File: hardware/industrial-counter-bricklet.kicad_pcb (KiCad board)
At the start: 2 copper layers, 40 x 40 mm, 44 parts, among them J1 DEBUG, P1 CON-SENSOR2, P2 BOOT, P3 CONN_8, U1 XMC1XXX48, U2 TLP2767, U3 TLP2767, U4 TLP2767, U5 TLP2767, U6 DRILL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

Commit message: change opto type
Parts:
- U2, U3, U4, U5: value TLP2767 -> TLP2367
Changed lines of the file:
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@@
       (effects (font (size 0.15 0.15) (thickness 0.0375)))
     )
-    (fp_text value TLP2767 (at 0 -0.5) (layer F.Fab)
+    (fp_text value TLP2367 (at 0 -0.5) (layer F.Fab)
       (effects (font (size 0.15 0.15) (thickness 0.0375)))
     )
@@
       (effects (font (size 0.15 0.15) (thickness 0.0375)))
     )
-    (fp_text value TLP2767 (at 0 -0.5) (layer F.Fab)
+    (fp_text value TLP2367 (at 0 -0.5) (layer F.Fab)
       (effects (font (size 0.15 0.15) (thickness 0.0375)))
     )
@@
       (effects (font (size 0.15 0.15) (thickness 0.0375)))
     )
-    (fp_text value TLP2767 (at 0 -0.5) (layer F.Fab)
+    (fp_text value TLP2367 (at 0 -0.5) (layer F.Fab)
       (effects (font (size 0.15 0.15) (thickness 0.0375)))
     )
@@
       (effects (font (size 0.15 0.15) (thickness 0.0375)))
     )
-    (fp_text value TLP2767 (at 0 -0.5) (layer F.Fab)
+    (fp_text value TLP2367 (at 0 -0.5) (layer F.Fab)
       (effects (font (size 0.15 0.15) (thickness 0.0375)))
     )

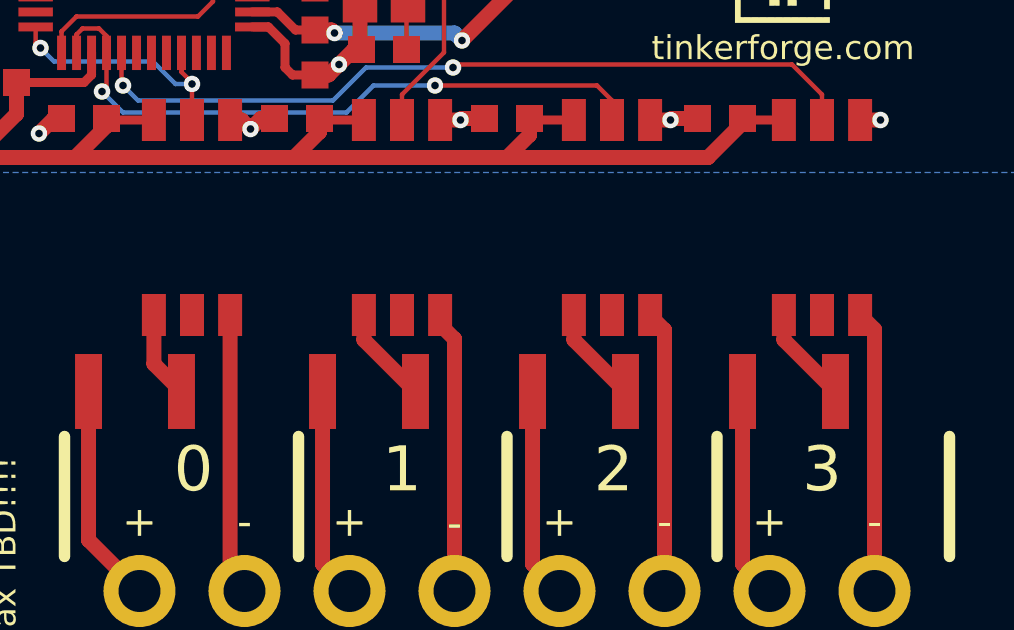
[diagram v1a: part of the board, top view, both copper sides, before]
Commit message: fix tlp2367 footprints
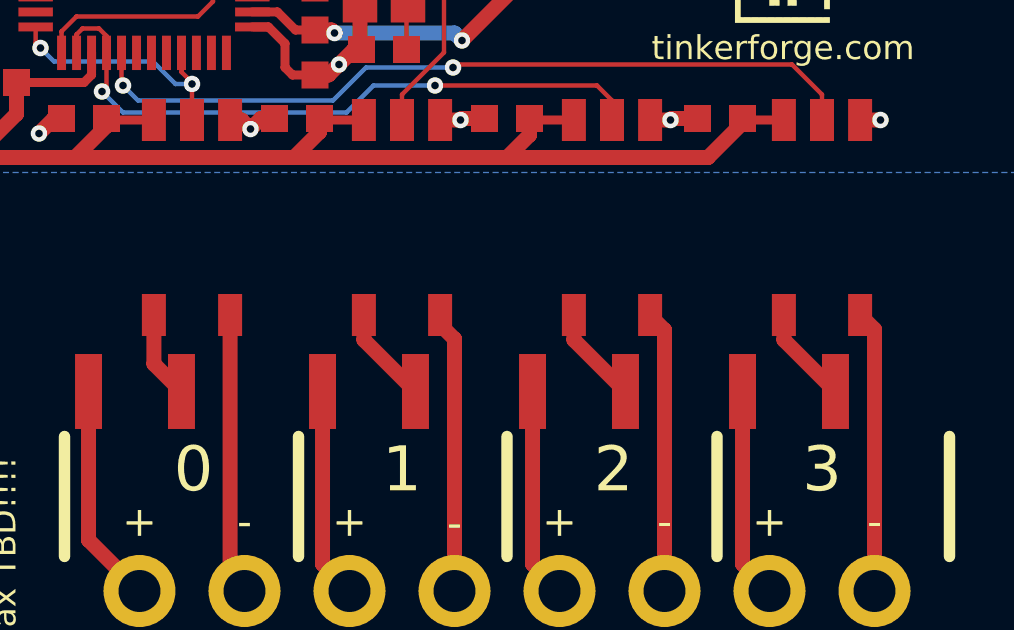
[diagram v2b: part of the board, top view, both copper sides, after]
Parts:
- U2, U3, U4, U5: footprint kicad-libraries:SO-6 -> kicad-libraries:SO-5
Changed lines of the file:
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@@
       (net 40 "Net-(J1-Pad1)"))
   )
-  (module kicad-libraries:SO-6 (layer Front)
+  (module kicad-libraries:SO-5 (layer Front)
+    (at 128.3 57.55)
+    (attr smd)
+    (fp_text reference U5 (at 0 0.5) (layer F.Fab)
+      (effects (font (size 0.15 0.15) (thickness 0.0375)))
+    )
+    (fp_text value TLP2367 (at 0 -0.5) (layer F.Fab)
+      (effects (font (size 0.15 0.15) (thickness 0.0375)))
+    )
+    (fp_circle (center -1.3 1.8) (end -1.2 1.9) (layer F.Fab) (width 0.15))
+    (fp_line (start -1.9 -2.3) (end 1.9 -2.3) (layer F.Fab) (width 0.15))
+    (fp_line (start 1.9 -2.3) (end 1.9 2.3) (layer F.Fab) (width 0.15))
+    (fp_line (start 1.9 2.3) (end -1.9 2.3) (layer F.Fab) (width 0.15))
+    (fp_line (start -1.9 2.3) (end -1.9 -2.3) (layer F.Fab) (width 0.15))
+    (pad 3 smd rect (at 1.27 3.25) (size 0.8 1.4) (layers Front F.Paste F.Mask)
+      (net 22 "Net-(P3-Pad8)"))
+    (pad 1 smd rect (at -1.27 3.25) (size 0.8 1.4) (layers Front F.Paste F.Mask)
+      (net 27 "Net-(R5-Pad2)"))
+    (pad 4 smd rect (at 1.27 -3.25) (size 0.8 1.4) (layers Front F.Paste F.Mask)
+      (net 1 GND))
+    (pad 5 smd rect (at 0 -3.25) (size 0.8 1.4) (layers Front F.Paste F.Mask)
+      (net 39 IN4))
+    (pad 6 smd rect (at -1.27 -3.25) (size 0.8 1.4) (layers Front F.Paste F.Mask)
+      (net 3 VCC))
+  )
+  (module kicad-libraries:SO-5 (layer Front)
+    (at 121.3 57.55)
+    (attr smd)
+    (fp_text reference U4 (at 0 0.5) (layer F.Fab)
+      (effects (font (size 0.15 0.15) (thickness 0.0375)))
+    )
+    (fp_text value TLP2367 (at 0 -0.5) (layer F.Fab)
+      (effects (font (size 0.15 0.15) (thickness 0.0375)))
+    )
+    (fp_circle (center -1.3 1.8) (end -1.2 1.9) (layer F.Fab) (width 0.15))
+    (fp_line (start -1.9 -2.3) (end 1.9 -2.3) (layer F.Fab) (width 0.15))
+    (fp_line (start 1.9 -2.3) (end 1.9 2.3) (layer F.Fab) (width 0.15))
+    (fp_line (start 1.9 2.3) (end -1.9 2.3) (layer F.Fab) (width 0.15))
+    (fp_line (start -1.9 2.3) (end -1.9 -2.3) (layer F.Fab) (width 0.15))
+    (pad 3 smd rect (at 1.27 3.25) (size 0.8 1.4) (layers Front F.Paste F.Mask)
+      (net 20 "Net-(P3-Pad6)"))
+    (pad 1 smd rect (at -1.27 3.25) (size 0.8 1.4) (layers Front F.Paste F.Mask)
+      (net 26 "Net-(R4-Pad2)"))
+    (pad 4 smd rect (at 1.27 -3.25) (size 0.8 1.4) (layers Front F.Paste F.Mask)
+      (net 1 GND))
+    (pad 5 smd rect (at 0 -3.25) (size 0.8 1.4) (layers Front F.Paste F.Mask)
+      (net 38 IN3))
+    (pad 6 smd rect (at -1.27 -3.25) (size 0.8 1.4) (layers Front F.Paste F.Mask)
+      (net 3 VCC))
+  )
+  (module kicad-libraries:SO-5 (layer Front)
+    (at 114.3 57.55)
+    (attr smd)
+    (fp_text reference U3 (at 0 0.5) (layer F.Fab)
+      (effects (font (size 0.15 0.15) (thickness 0.0375)))
+    )
+    (fp_text value TLP2367 (at 0 -0.5) (layer F.Fab)
+      (effects (font (size 0.15 0.15) (thickness 0.0375)))
+    )
+    (fp_circle (center -1.3 1.8) (end -1.2 1.9) (layer F.Fab) (width 0.15))
+    (fp_line (start -1.9 -2.3) (end 1.9 -2.3) (layer F.Fab) (width 0.15))
+    (fp_line (start 1.9 -2.3) (end 1.9 2.3) (layer F.Fab) (width 0.15))
+    (fp_line (start 1.9 2.3) (end -1.9 2.3) (layer F.Fab) (width 0.15))
+    (fp_line (start -1.9 2.3) (end -1.9 -2.3) (layer F.Fab) (width 0.15))
+    (pad 3 smd rect (at 1.27 3.25) (size 0.8 1.4) (layers Front F.Paste F.Mask)
+      (net 17 "Net-(P3-Pad4)"))
+    (pad 1 smd rect (at -1.27 3.25) (size 0.8 1.4) (layers Front F.Paste F.Mask)
+      (net 25 "Net-(R3-Pad2)"))
+    (pad 4 smd rect (at 1.27 -3.25) (size 0.8 1.4) (layers Front F.Paste F.Mask)
+      (net 1 GND))
+    (pad 5 smd rect (at 0 -3.25) (size 0.8 1.4) (layers Front F.Paste F.Mask)
+      (net 37 IN2))
+    (pad 6 smd rect (at -1.27 -3.25) (size 0.8 1.4) (layers Front F.Paste F.Mask)
+      (net 3 VCC))
+  )
+  (module kicad-libraries:SO-5 (layer Front)
     (at 107.3 57.55)
+    (attr smd)
     (fp_text reference U2 (at 0 0.5) (layer F.Fab)
       (effects (font (size 0.15 0.15) (thickness 0.0375)))
@@
     (fp_line (start 1.9 2.3) (end -1.9 2.3) (layer F.Fab) (width 0.15))
     (fp_line (start -1.9 2.3) (end -1.9 -2.3) (layer F.Fab) (width 0.15))
-    (pad 2 smd rect (at 0 3.25) (size 0.8 1.4) (layers Front F.Paste F.Mask))
     (pad 3 smd rect (at 1.27 3.25) (size 0.8 1.4) (layers Front F.Paste F.Mask)
       (net 15 "Net-(P3-Pad2)"))
@@
     (pad 6 smd rect (at -1.27 -3.25) (size 0.8 1.4) (layers Front F.Paste F.Mask)
       (net 3 VCC))
-  )
-  (module kicad-libraries:SO-6 (layer Front)
-    (at 114.3 57.55)
-    (fp_text reference U3 (at 0 0.5) (layer F.Fab)
-      (effects (font (size 0.15 0.15) (thickness 0.0375)))
-    )
-    (fp_text value TLP2367 (at 0 -0.5) (layer F.Fab)
-      (effects (font (size 0.15 0.15) (thickness 0.0375)))
-    )
-    (fp_circle (center -1.3 1.8) (end -1.2 1.9) (layer F.Fab) (width 0.15))
-    (fp_line (start -1.9 -2.3) (end 1.9 -2.3) (layer F.Fab) (width 0.15))
-    (fp_line (start 1.9 -2.3) (end 1.9 2.3) (layer F.Fab) (width 0.15))
-    (fp_line (start 1.9 2.3) (end -1.9 2.3) (layer F.Fab) (width 0.15))
-    (fp_line (start -1.9 2.3) (end -1.9 -2.3) (layer F.Fab) (width 0.15))
-    (pad 2 smd rect (at 0 3.25) (size 0.8 1.4) (layers Front F.Paste F.Mask))
-    (pad 3 smd rect (at 1.27 3.25) (size 0.8 1.4) (layers Front F.Paste F.Mask)
-      (net 17 "Net-(P3-Pad4)"))
-    (pad 1 smd rect (at -1.27 3.25) (size 0.8 1.4) (layers Front F.Paste F.Mask)
-      (net 25 "Net-(R3-Pad2)"))
-    (pad 4 smd rect (at 1.27 -3.25) (size 0.8 1.4) (layers Front F.Paste F.Mask)
-      (net 1 GND))
-    (pad 5 smd rect (at 0 -3.25) (size 0.8 1.4) (layers Front F.Paste F.Mask)
-      (net 37 IN2))
-    (pad 6 smd rect (at -1.27 -3.25) (size 0.8 1.4) (layers Front F.Paste F.Mask)
-      (net 3 VCC))
-  )
-  (module kicad-libraries:SO-6 (layer Front)
-    (at 121.3 57.55)
-    (fp_text reference U4 (at 0 0.5) (layer F.Fab)
-      (effects (font (size 0.15 0.15) (thickness 0.0375)))
-    )
-    (fp_text value TLP2367 (at 0 -0.5) (layer F.Fab)
-      (effects (font (size 0.15 0.15) (thickness 0.0375)))
-    )
-    (fp_circle (center -1.3 1.8) (end -1.2 1.9) (layer F.Fab) (width 0.15))
-    (fp_line (start -1.9 -2.3) (end 1.9 -2.3) (layer F.Fab) (width 0.15))
-    (fp_line (start 1.9 -2.3) (end 1.9 2.3) (layer F.Fab) (width 0.15))
-    (fp_line (start 1.9 2.3) (end -1.9 2.3) (layer F.Fab) (width 0.15))
-    (fp_line (start -1.9 2.3) (end -1.9 -2.3) (layer F.Fab) (width 0.15))
-    (pad 2 smd rect (at 0 3.25) (size 0.8 1.4) (layers Front F.Paste F.Mask))
-    (pad 3 smd rect (at 1.27 3.25) (size 0.8 1.4) (layers Front F.Paste F.Mask)
-      (net 20 "Net-(P3-Pad6)"))
-    (pad 1 smd rect (at -1.27 3.25) (size 0.8 1.4) (layers Front F.Paste F.Mask)
-      (net 26 "Net-(R4-Pad2)"))
-    (pad 4 smd rect (at 1.27 -3.25) (size 0.8 1.4) (layers Front F.Paste F.Mask)
-      (net 1 GND))
-    (pad 5 smd rect (at 0 -3.25) (size 0.8 1.4) (layers Front F.Paste F.Mask)
-      (net 38 IN3))
-    (pad 6 smd rect (at -1.27 -3.25) (size 0.8 1.4) (layers Front F.Paste F.Mask)
-      (net 3 VCC))
-  )
-  (module kicad-libraries:SO-6 (layer Front)
-    (at 128.3 57.55)
-    (fp_text reference U5 (at 0 0.5) (layer F.Fab)
-      (effects (font (size 0.15 0.15) (thickness 0.0375)))
-    )
-    (fp_text value TLP2367 (at 0 -0.5) (layer F.Fab)
-      (effects (font (size 0.15 0.15) (thickness 0.0375)))
-    )
-    (fp_circle (center -1.3 1.8) (end -1.2 1.9) (layer F.Fab) (width 0.15))
-    (fp_line (start -1.9 -2.3) (end 1.9 -2.3) (layer F.Fab) (width 0.15))
-    (fp_line (start 1.9 -2.3) (end 1.9 2.3) (layer F.Fab) (width 0.15))
-    (fp_line (start 1.9 2.3) (end -1.9 2.3) (layer F.Fab) (width 0.15))
-    (fp_line (start -1.9 2.3) (end -1.9 -2.3) (layer F.Fab) (width 0.15))
-    (pad 2 smd rect (at 0 3.25) (size 0.8 1.4) (layers Front F.Paste F.Mask))
-    (pad 3 smd rect (at 1.27 3.25) (size 0.8 1.4) (layers Front F.Paste F.Mask)
-      (net 22 "Net-(P3-Pad8)"))
-    (pad 1 smd rect (at -1.27 3.25) (size 0.8 1.4) (layers Front F.Paste F.Mask)
-      (net 27 "Net-(R5-Pad2)"))
-    (pad 4 smd rect (at 1.27 -3.25) (size 0.8 1.4) (layers Front F.Paste F.Mask)
-      (net 1 GND))
-    (pad 5 smd rect (at 0 -3.25) (size 0.8 1.4) (layers Front F.Paste F.Mask)
-      (net 39 IN4))
-    (pad 6 smd rect (at -1.27 -3.25) (size 0.8 1.4) (layers Front F.Paste F.Mask)
-      (net 3 VCC))

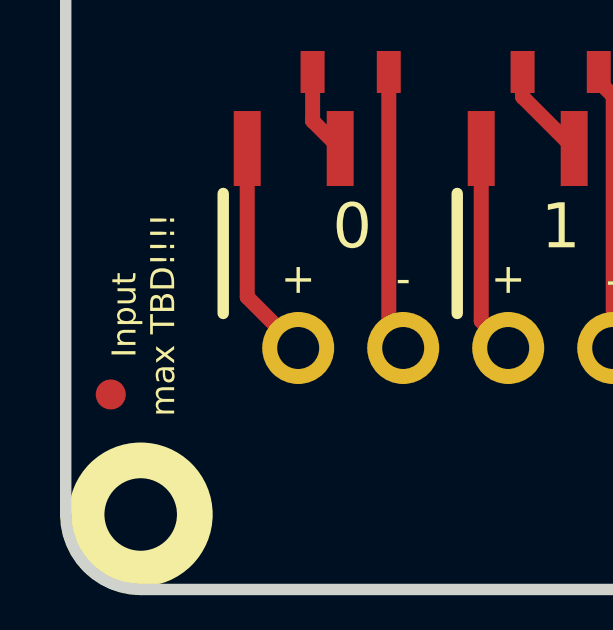
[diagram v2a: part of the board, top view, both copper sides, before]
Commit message: specify resistor values and input range
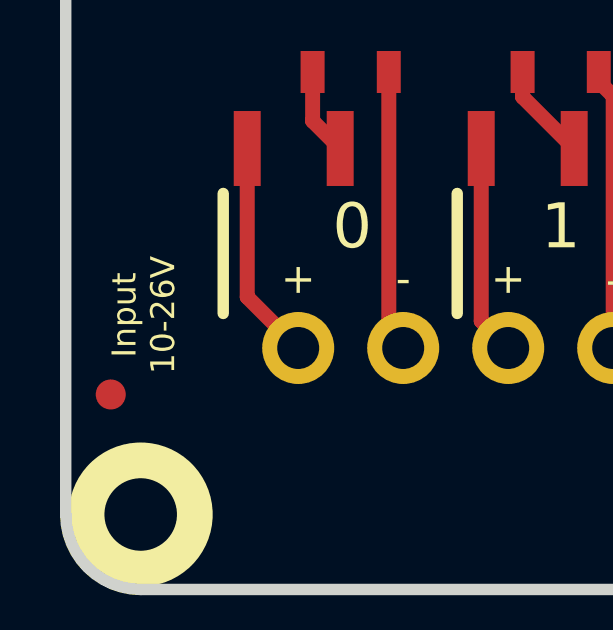
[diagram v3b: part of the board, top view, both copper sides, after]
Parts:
- R2, R3, R4, R5: value 4.7k -> 2.7k 0.5W
- U2, U3, U4, U5: footprint kicad-libraries:SO-5 -> SO-5
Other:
- board text added: "Input 10-26V"
- board text removed: "Input max TBD!!!!"
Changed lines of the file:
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@@
     (links 95)
     (no_connects 0)
-    (area 96.945139 37.195139 281.34585 165.190793)
+    (area 97.609659 37.858699 137.993121 78.242161)
     (thickness 1.6002)
     (drawings 34)
@@
       (effects (font (size 0.29972 0.29972) (thickness 0.07493)))
     )
-    (fp_text value 4.7k (at 0 0.54) (layer F.Fab)
+    (fp_text value "2.7k 0.5W" (at 0 0.54) (layer F.Fab)
       (effects (font (size 0.29972 0.29972) (thickness 0.07493)))
     )
@@
       (effects (font (size 0.29972 0.29972) (thickness 0.07493)))
     )
-    (fp_text value 4.7k (at 0 0.54) (layer F.Fab)
+    (fp_text value "2.7k 0.5W" (at 0 0.54) (layer F.Fab)
       (effects (font (size 0.29972 0.29972) (thickness 0.07493)))
     )
@@
       (effects (font (size 0.29972 0.29972) (thickness 0.07493)))
     )
-    (fp_text value 4.7k (at 0 0.54) (layer F.Fab)
+    (fp_text value "2.7k 0.5W" (at 0 0.54) (layer F.Fab)
       (effects (font (size 0.29972 0.29972) (thickness 0.07493)))
     )
@@
       (effects (font (size 0.29972 0.29972) (thickness 0.07493)))
     )
-    (fp_text value 4.7k (at 0 0.54) (layer F.Fab)
+    (fp_text value "2.7k 0.5W" (at 0 0.54) (layer F.Fab)
       (effects (font (size 0.29972 0.29972) (thickness 0.07493)))
     )
@@
       (net 40 "Net-(J1-Pad1)"))
   )
-  (module kicad-libraries:SO-5 (layer Front)
-    (at 128.3 57.55)
+  (module SO-5 (layer Front)
+    (at 107.3 57.55)
     (attr smd)
-    (fp_text reference U5 (at 0 0.5) (layer F.Fab)
+    (fp_text reference U2 (at 0 0.5) (layer F.Fab)
       (effects (font (size 0.15 0.15) (thickness 0.0375)))
     )
@@
     (fp_line (start -1.9 2.3) (end -1.9 -2.3) (layer F.Fab) (width 0.15))
     (pad 3 smd rect (at 1.27 3.25) (size 0.8 1.4) (layers Front F.Paste F.Mask)
-      (net 22 "Net-(P3-Pad8)"))
+      (net 15 "Net-(P3-Pad2)"))
     (pad 1 smd rect (at -1.27 3.25) (size 0.8 1.4) (layers Front F.Paste F.Mask)
-      (net 27 "Net-(R5-Pad2)"))
+      (net 24 "Net-(R2-Pad2)"))
     (pad 4 smd rect (at 1.27 -3.25) (size 0.8 1.4) (layers Front F.Paste F.Mask)
       (net 1 GND))
     (pad 5 smd rect (at 0 -3.25) (size 0.8 1.4) (layers Front F.Paste F.Mask)
-      (net 39 IN4))
+      (net 36 IN1))
     (pad 6 smd rect (at -1.27 -3.25) (size 0.8 1.4) (layers Front F.Paste F.Mask)
       (net 3 VCC))
   )
-  (module kicad-libraries:SO-5 (layer Front)
-    (at 121.3 57.55)
+  (module SO-5 (layer Front)
+    (at 114.3 57.55)
     (attr smd)
-    (fp_text reference U4 (at 0 0.5) (layer F.Fab)
+    (fp_text reference U3 (at 0 0.5) (layer F.Fab)
       (effects (font (size 0.15 0.15) (thickness 0.0375)))
     )
@@
     (fp_line (start -1.9 2.3) (end -1.9 -2.3) (layer F.Fab) (width 0.15))
     (pad 3 smd rect (at 1.27 3.25) (size 0.8 1.4) (layers Front F.Paste F.Mask)
-      (net 20 "Net-(P3-Pad6)"))
+      (net 17 "Net-(P3-Pad4)"))
     (pad 1 smd rect (at -1.27 3.25) (size 0.8 1.4) (layers Front F.Paste F.Mask)
-      (net 26 "Net-(R4-Pad2)"))
+      (net 25 "Net-(R3-Pad2)"))
     (pad 4 smd rect (at 1.27 -3.25) (size 0.8 1.4) (layers Front F.Paste F.Mask)
       (net 1 GND))
     (pad 5 smd rect (at 0 -3.25) (size 0.8 1.4) (layers Front F.Paste F.Mask)
-      (net 38 IN3))
+      (net 37 IN2))
     (pad 6 smd rect (at -1.27 -3.25) (size 0.8 1.4) (layers Front F.Paste F.Mask)
       (net 3 VCC))
   )
-  (module kicad-libraries:SO-5 (layer Front)
-    (at 114.3 57.55)
+  (module SO-5 (layer Front)
+    (at 121.3 57.55)
     (attr smd)
-    (fp_text reference U3 (at 0 0.5) (layer F.Fab)
+    (fp_text reference U4 (at 0 0.5) (layer F.Fab)
       (effects (font (size 0.15 0.15) (thickness 0.0375)))
     )
@@
     (fp_line (start -1.9 2.3) (end -1.9 -2.3) (layer F.Fab) (width 0.15))
     (pad 3 smd rect (at 1.27 3.25) (size 0.8 1.4) (layers Front F.Paste F.Mask)
-      (net 17 "Net-(P3-Pad4)"))
+      (net 20 "Net-(P3-Pad6)"))
     (pad 1 smd rect (at -1.27 3.25) (size 0.8 1.4) (layers Front F.Paste F.Mask)
-      (net 25 "Net-(R3-Pad2)"))
+      (net 26 "Net-(R4-Pad2)"))
     (pad 4 smd rect (at 1.27 -3.25) (size 0.8 1.4) (layers Front F.Paste F.Mask)
       (net 1 GND))
     (pad 5 smd rect (at 0 -3.25) (size 0.8 1.4) (layers Front F.Paste F.Mask)
-      (net 37 IN2))
+      (net 38 IN3))
     (pad 6 smd rect (at -1.27 -3.25) (size 0.8 1.4) (layers Front F.Paste F.Mask)
       (net 3 VCC))
   )
-  (module kicad-libraries:SO-5 (layer Front)
-    (at 107.3 57.55)
+  (module SO-5 (layer Front)
+    (at 128.3 57.55)
     (attr smd)
-    (fp_text reference U2 (at 0 0.5) (layer F.Fab)
+    (fp_text reference U5 (at 0 0.5) (layer F.Fab)
       (effects (font (size 0.15 0.15) (thickness 0.0375)))
     )
@@
     (fp_line (start -1.9 2.3) (end -1.9 -2.3) (layer F.Fab) (width 0.15))
     (pad 3 smd rect (at 1.27 3.25) (size 0.8 1.4) (layers Front F.Paste F.Mask)
-      (net 15 "Net-(P3-Pad2)"))
+      (net 22 "Net-(P3-Pad8)"))
     (pad 1 smd rect (at -1.27 3.25) (size 0.8 1.4) (layers Front F.Paste F.Mask)
-      (net 24 "Net-(R2-Pad2)"))
+      (net 27 "Net-(R5-Pad2)"))
     (pad 4 smd rect (at 1.27 -3.25) (size 0.8 1.4) (layers Front F.Paste F.Mask)
       (net 1 GND))
     (pad 5 smd rect (at 0 -3.25) (size 0.8 1.4) (layers Front F.Paste F.Mask)
-      (net 36 IN1))
+      (net 39 IN4))
     (pad 6 smd rect (at -1.27 -3.25) (size 0.8 1.4) (layers Front F.Paste F.Mask)
       (net 3 VCC))
@@
     (effects (font (size 0.8001 0.8001) (thickness 0.200025)))
   )
-  (gr_text "Input\nmax TBD!!!!" (at 100.4 68.9 90) (layer F.SilkS)
+  (gr_text "Input\n10-26V" (at 100.4 68.9 90) (layer F.SilkS)
     (effects (font (size 0.8001 0.8001) (thickness 0.14986)))
   )

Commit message: fix logos
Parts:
- added G***: LOGO, kicad-libraries:Logo_CoMCU, B.Cu at (127.8, 58.0)
- moved VAL 7.10 mm to (107.8, 58.0), turned to 90 degrees
- moved VAL 3.00 mm to (117.8, 58.0), turned to 90 degrees
